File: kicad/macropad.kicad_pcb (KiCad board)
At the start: 2 copper layers, 109.5 x 92 mm, 15 parts, among them J1 Conn_01x04_Socket, SW1 CherryMX, SW10 RotaryEncoder_Switch, SW11 RotaryEncoder_Switch, SW12 SW_Push, SW2 CherryMX, SW3 CherryMX, SW4 CherryMX, SW5 CherryMX, SW6 CherryMX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

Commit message: updated design
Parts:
- added REF**: Macropad_EdgeCut, Macropad_Library:Macropad_EdgeCut, F.Cu at (128.5, 40.5)
- SW10, SW11: footprint Rotary_Encoder:RotaryEncoder_Alps_EC11E-Switch_Vertical_H20mm -> Macropad_Library:RotaryEncoder
- U1: footprint footprints:RPi_Pico_SMD_TH -> Macropad_Library:RPi_Pico_SMD_TH
- moved SW10 9.69 mm to (143.5, 101.5)
- moved SW11 9.42 mm to (143.5, 82.5)
- moved SW12 8.17 mm to (143.5, 64.5)
- moved U2 4.50 mm to (143.5, 119.5)
- moved J1 4.16 mm to (173.7, 54.7)
- moved SW1 3.68 mm to (174.4, 76.3)
- moved SW4 3.68 mm to (193.5, 76.3)
- moved SW7 3.68 mm to (212.6, 76.3)
- moved SW2 3.68 mm to (174.4, 95.4)
- moved SW3 3.68 mm to (174.4, 114.4)
- moved SW5 3.68 mm to (193.5, 95.4)
- moved SW6 3.68 mm to (193.5, 114.4)
- moved SW8 3.68 mm to (212.6, 95.4)
- moved SW9 3.68 mm to (212.6, 114.4)
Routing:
- net Net-(U1-GPIO8): track 147.1 -> 115.8 mm
- net Net-(U1-GPIO7): track 146.0 -> 119.5 mm, vias 3 -> 1
- net Net-(U1-GPIO3): track 128.7 -> 118.1 mm, vias 3 -> 1
- net Net-(U1-GPIO6): track 126.3 -> 116.0 mm, vias 3 -> 1
- net 3v3: track 57.8 -> 49.7 mm
- net Net-(U1-GPIO22): track 59.3 -> 54.2 mm
- net GND: track 4.50 -> 0.00 mm
- net Net-(J1-Pin_2): track 46.6 -> 42.2 mm
- net Net-(U1-GPIO10): track 89.6 -> 85.4 mm
- net Net-(U1-GPIO19): track 37.3 -> 33.5 mm
- net Net-(U1-GPIO28_ADC2): track 65.7 -> 62.4 mm
- net Net-(U1-GPIO20): track 101.6 -> 98.4 mm
- net Net-(U1-GPIO21): track 80.8 -> 77.7 mm
- net Net-(U1-GPIO9): track 114.0 -> 111.0 mm
- net Net-(U1-GPIO17): track 17.3 -> 14.4 mm
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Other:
- board size 109.5 x 92 mm -> 100 x 92 mm

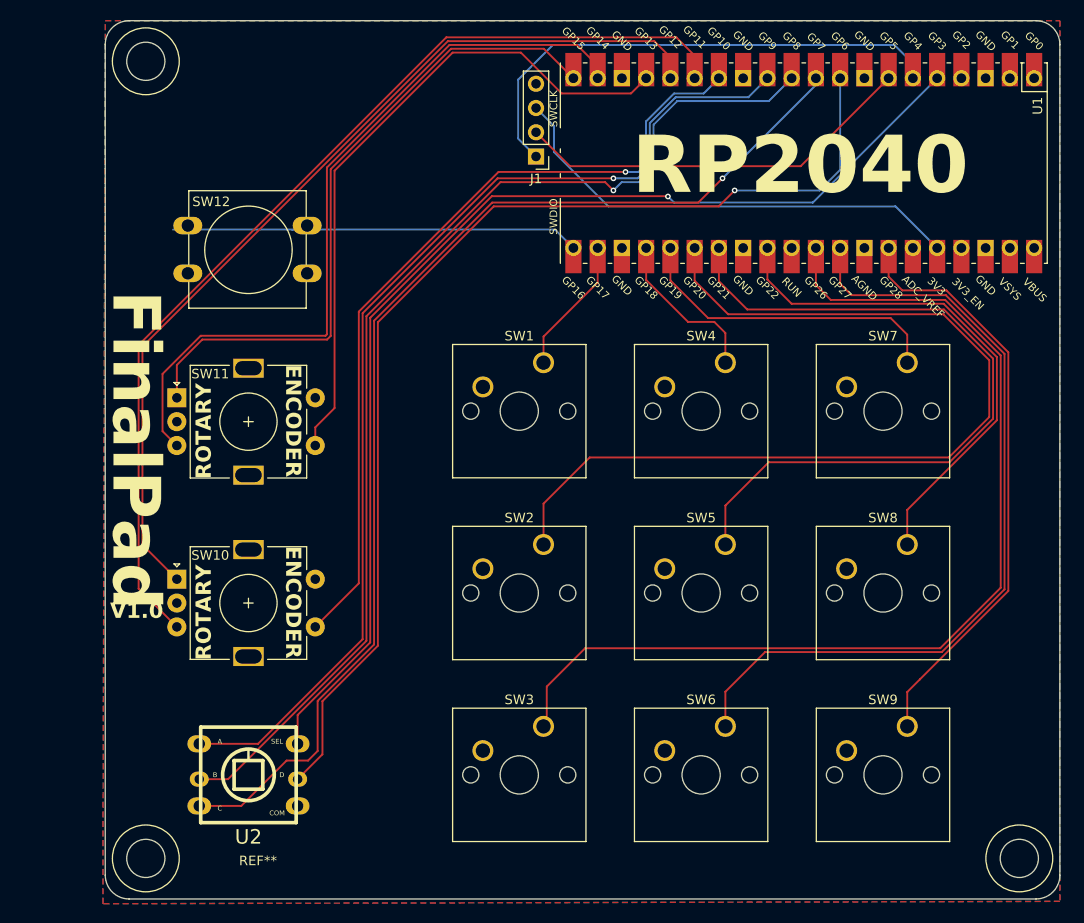
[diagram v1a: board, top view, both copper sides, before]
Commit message: added 3D models
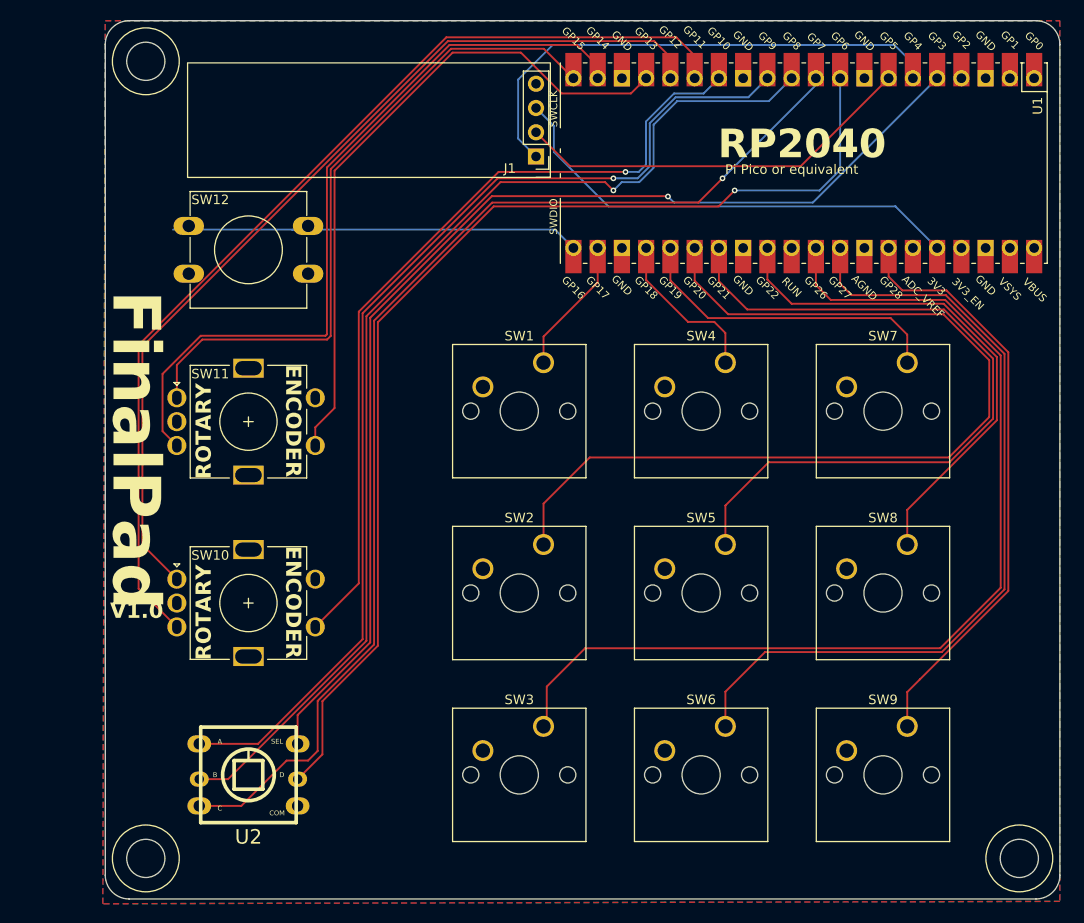
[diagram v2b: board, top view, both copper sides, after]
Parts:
- J1: footprint Connector_PinHeader_2.54mm:PinHeader_1x04_P2.54mm_Vertical -> Macropad_Library:SSD1306
- SW1, SW2, SW3, SW4, SW5, SW6, SW7, SW8, SW9: footprint Button_Switch_Keyboard:SW_Cherry_MX_1.00u_PCB -> Macropad_Library:SW_Cherry_MX_1.00u_PCB
- SW12: footprint Button_Switch_THT:SW_PUSH-12mm -> Macropad_Library:SW_PUSH-12mm

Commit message: updated silkscreen and moved switches up
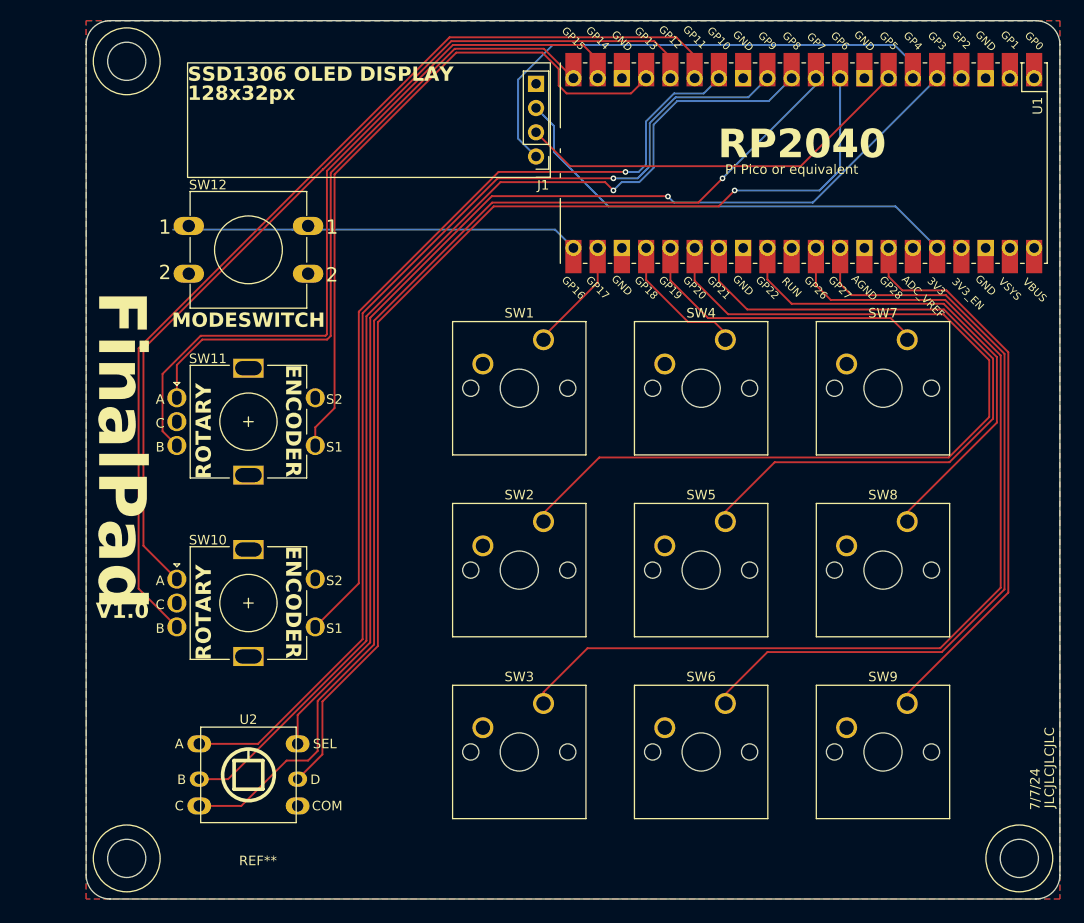
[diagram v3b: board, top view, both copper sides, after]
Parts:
- U2: footprint skqucaa010_joystick:SKQUCAA010 -> Macropad_Library:SKQUCAA010
- moved SW2 2.40 mm to (174.4, 93.0)
- moved SW3 2.40 mm to (174.4, 112.0)
- moved SW5 2.40 mm to (193.5, 93.0)
- moved SW6 2.40 mm to (193.5, 112.0)
- moved SW8 2.40 mm to (212.6, 93.0)
- moved SW9 2.40 mm to (212.6, 112.0)
- moved SW1 2.40 mm to (174.4, 73.9)
- moved SW4 2.40 mm to (193.5, 73.9)
- moved SW7 2.40 mm to (212.6, 73.9)
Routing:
- net Net-(U1-GPIO21): track 77.7 -> 73.9 mm
- net Net-(U1-GPIO27_ADC1): track 86.0 -> 82.5 mm
- net Net-(U1-GPIO28_ADC2): track 62.4 -> 59.0 mm
- net Net-(U1-GPIO20): track 98.4 -> 95.4 mm
- net Net-(U1-GPIO19): track 33.5 -> 30.6 mm
- net Net-(U1-GPIO26_ADC0): track 106.8 -> 104.2 mm
- net Net-(U1-GPIO22): track 54.2 -> 51.8 mm
- net Net-(U1-GPIO18): track 17.1 -> 14.7 mm
- net Net-(U1-GPIO17): track 14.4 -> 12.0 mm
- net Net-(U1-GPIO13): track 69.8 -> 70.6 mm
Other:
- board size 100 x 92 mm -> 102 x 92 mm
